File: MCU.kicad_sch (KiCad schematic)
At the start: 18 parts, among them J12 USB, U5 THVD1420DRLR, U6 CH32X035G8U6

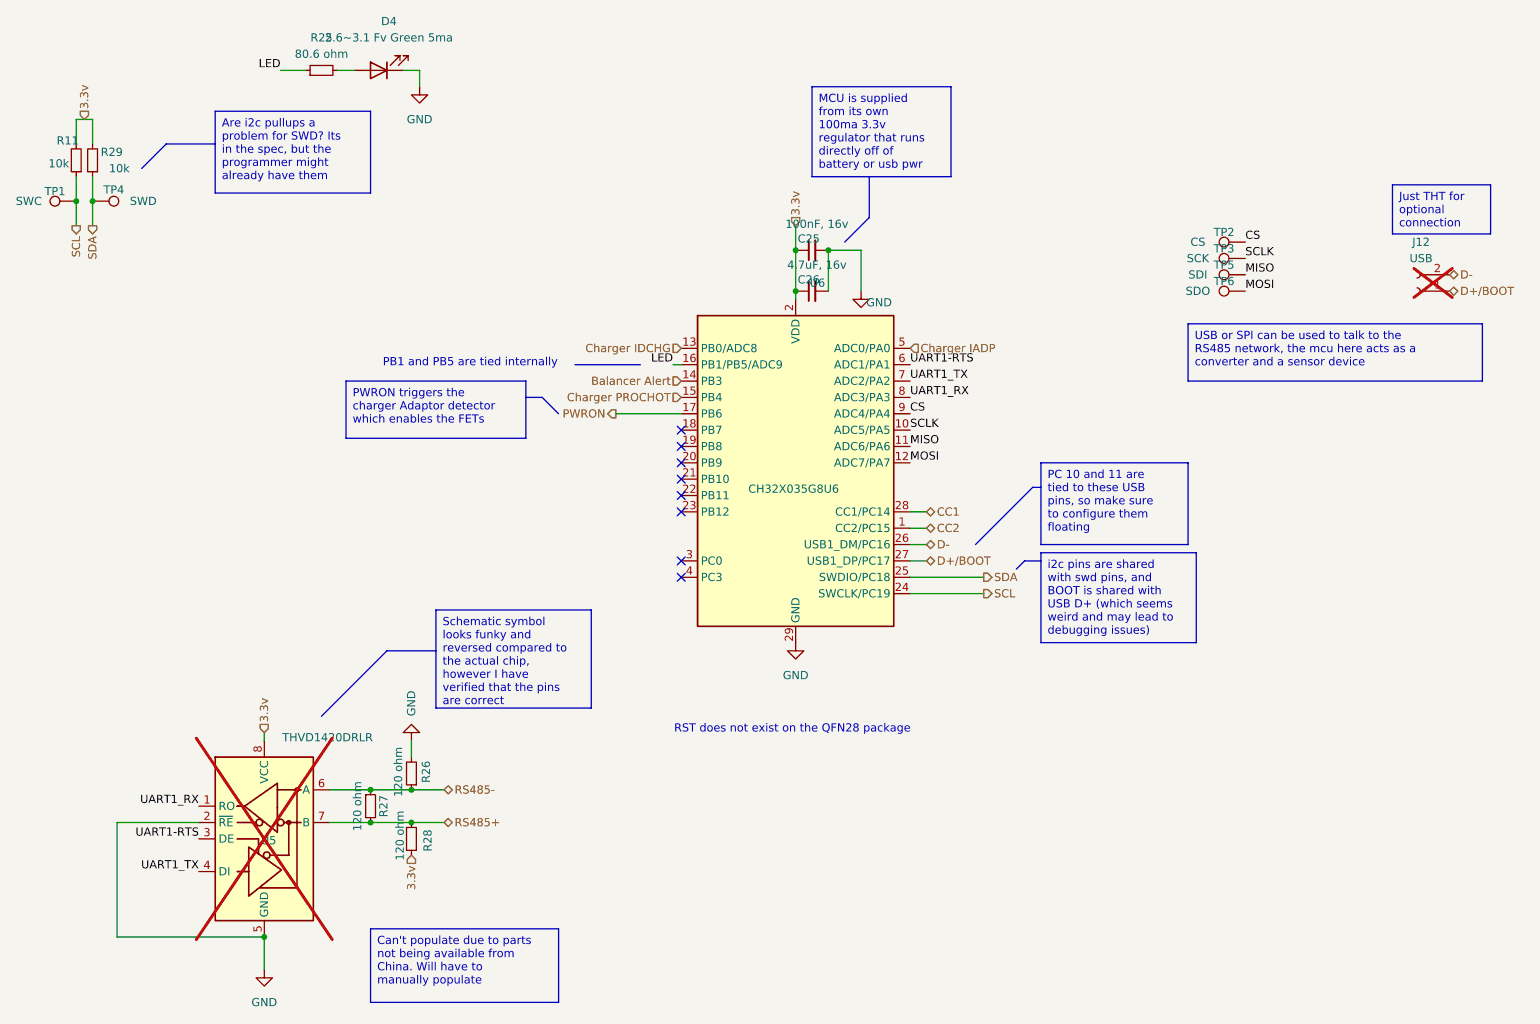
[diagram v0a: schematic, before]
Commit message: Updated to kicad 9
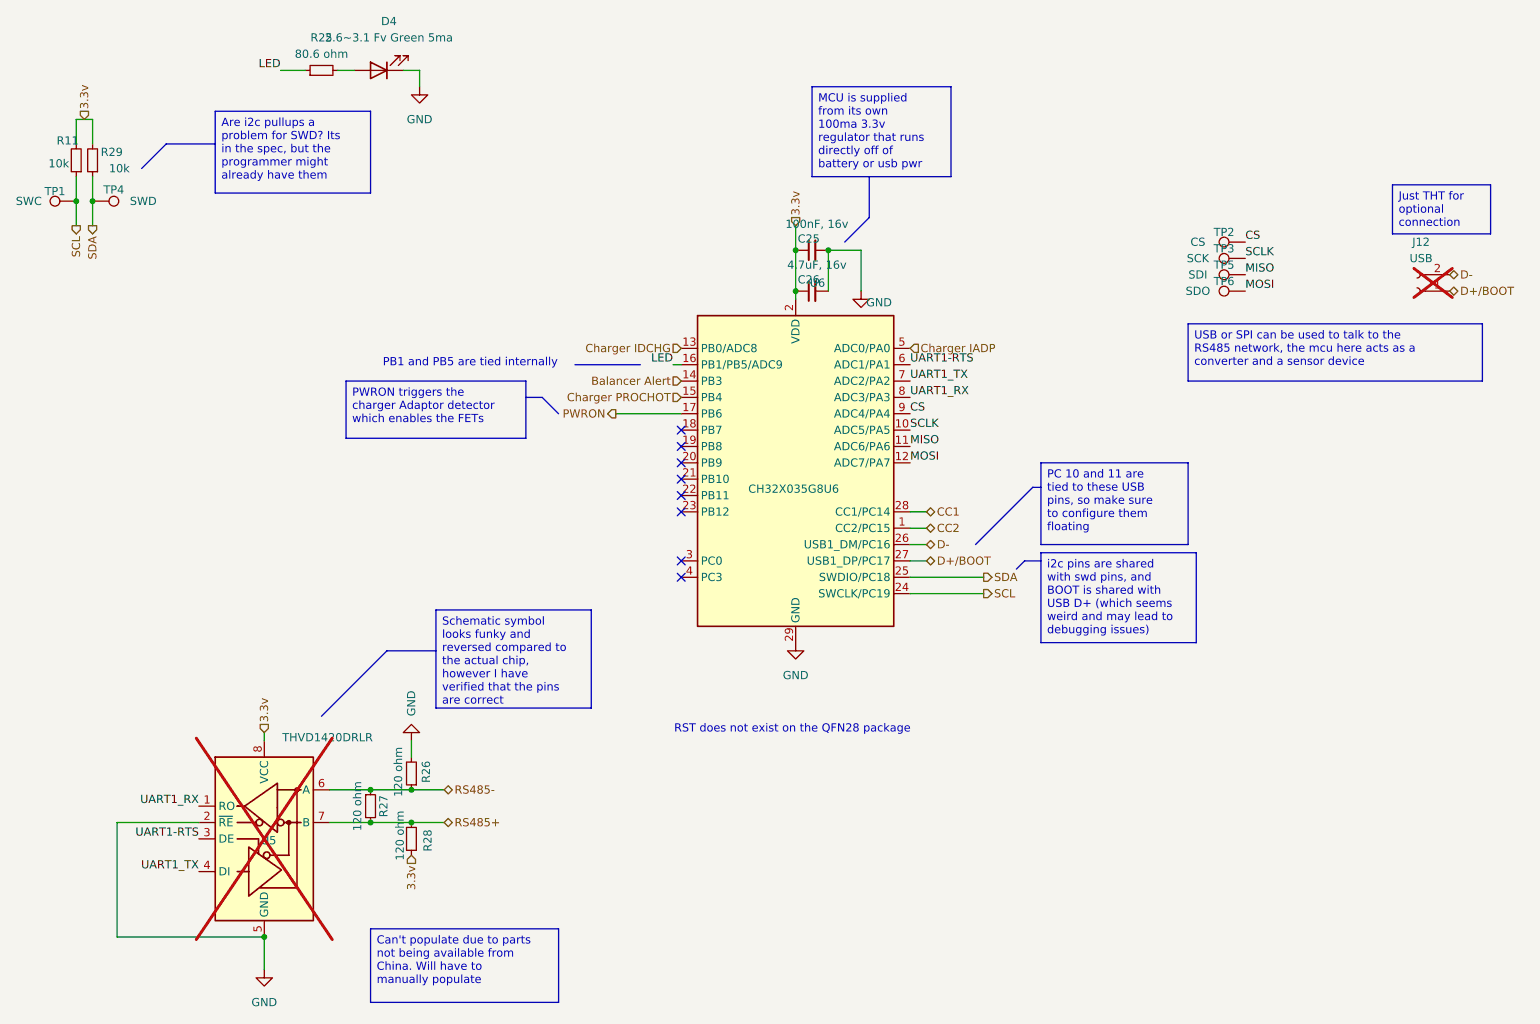
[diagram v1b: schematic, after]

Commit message: Added MCU boot button, 3v3 power enable, and pulldown on adaptor enable
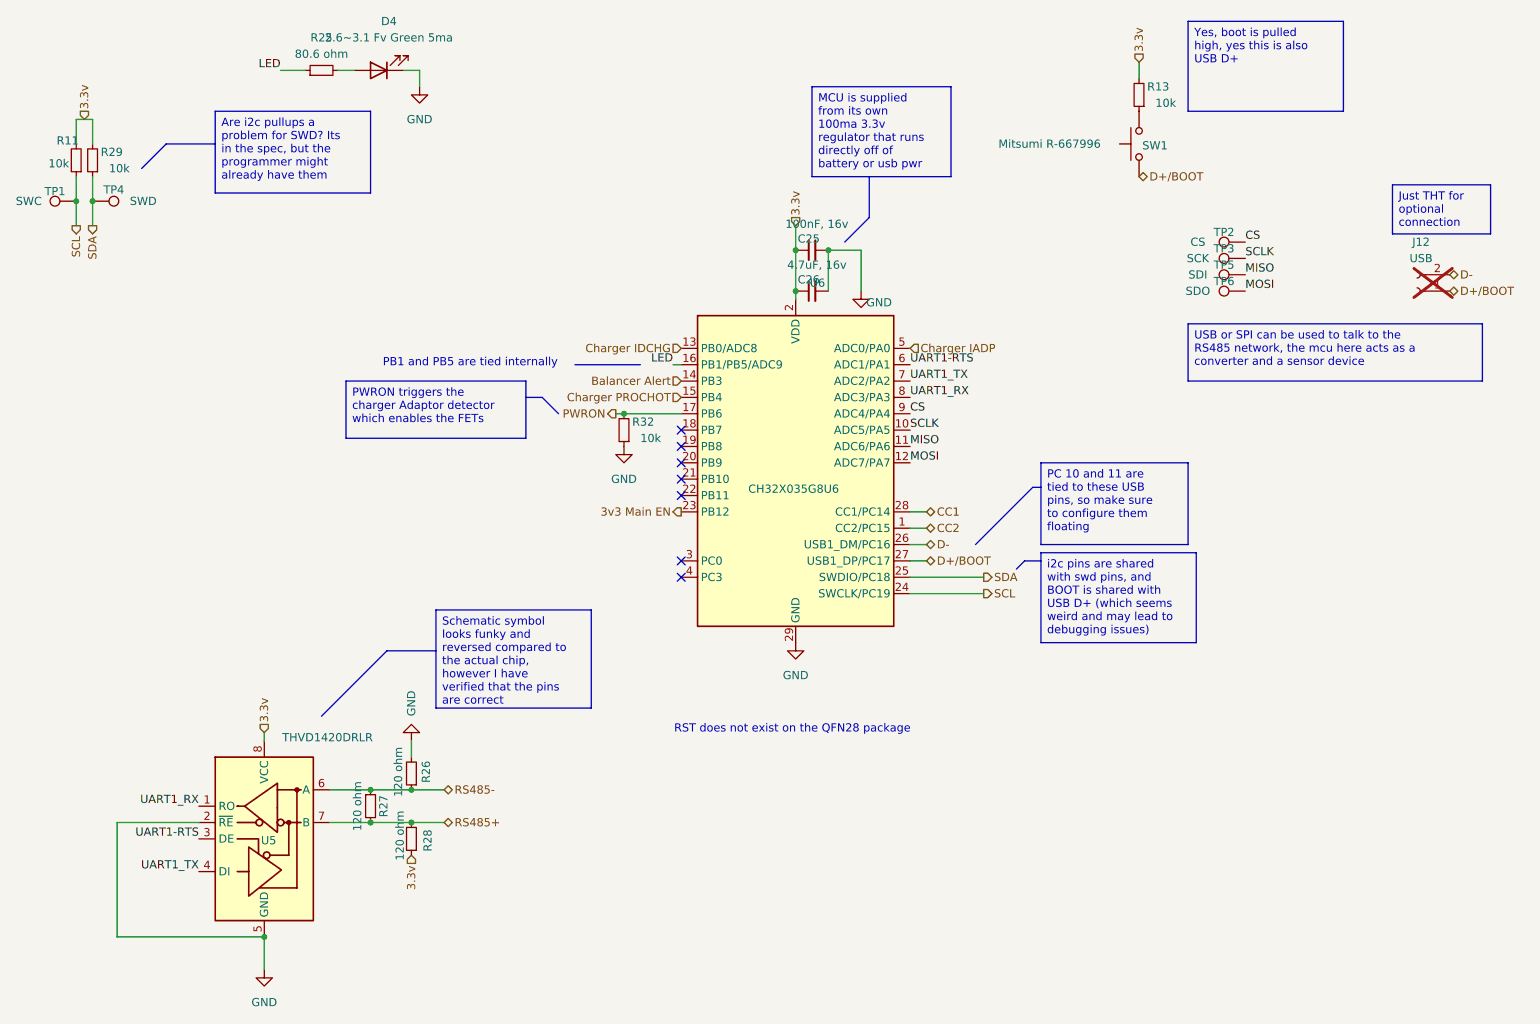
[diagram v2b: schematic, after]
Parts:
- added R13, R32: 10k, Resistor_SMD:R_0402_1005Metric, symbol Device:R_Small
- added SW1: Mitsumi R-667996, Misumi switches:R-667995_MIT, symbol Switch:SW_Push
- U5: now fitted
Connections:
- net 3.3v: now also R13.2
- net D+/BOOT: now also SW1.1
- net GND: now also R32.1
- net PWRON: now also R32.2
- net 3v3 Main EN: now reaches U6.23 (PB12)
- new net: R13.1, SW1.2
- no-connect marks 8 -> 7

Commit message: Added pdf schematics
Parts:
- U6: footprint Package_DFN_QFN:QFN-28-1EP_4x4mm_P0.4mm_EP2.8x2.8mm -> qfn_custom:QFN-28-1EP_4x4mm_P0.4mm_EP2.8x2.8mm
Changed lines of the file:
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@@
 			)
 		)
-		(property "Footprint" "Package_DFN_QFN:QFN-28-1EP_4x4mm_P0.4mm_EP2.8x2.8mm"
+		(property "Footprint" "qfn_custom:QFN-28-1EP_4x4mm_P0.4mm_EP2.8x2.8mm"
 			(at 146.05 142.24 0)
 			(effects

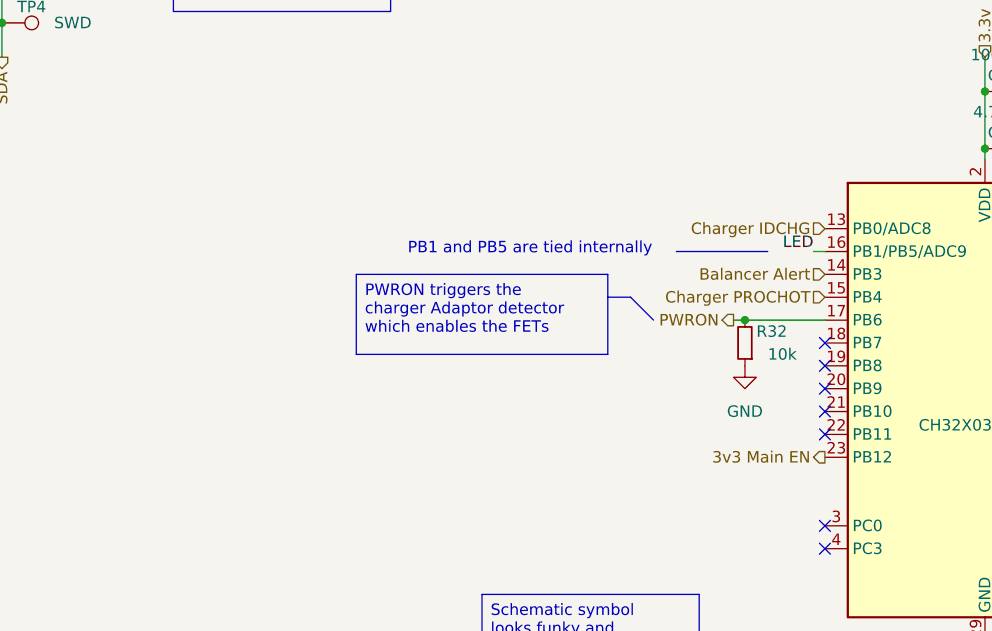
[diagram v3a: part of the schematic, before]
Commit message: Re order LED and enable pins
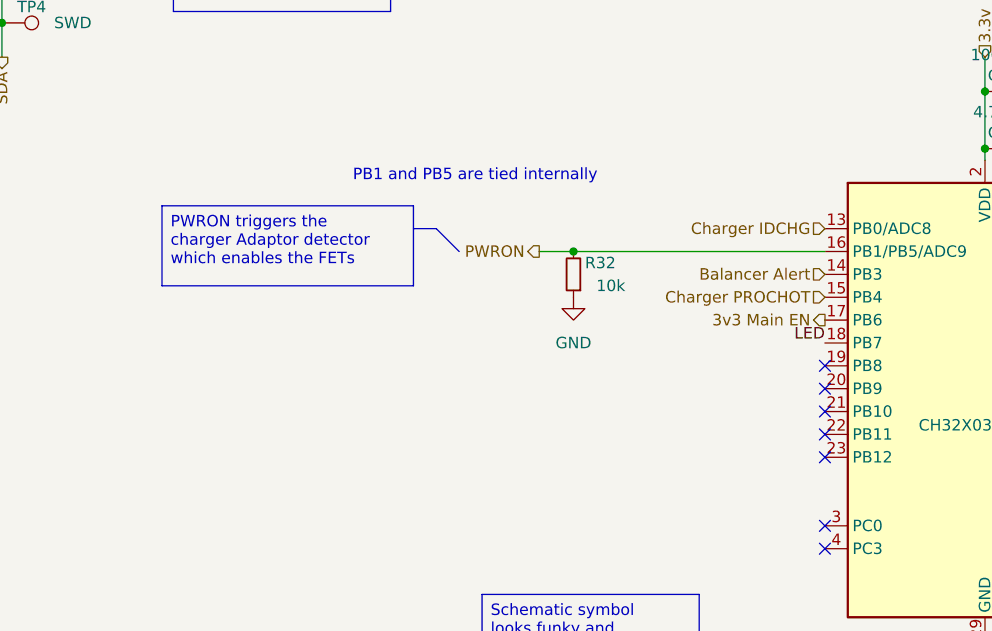
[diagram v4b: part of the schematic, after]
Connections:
- net 3v3 Main EN: now also U6.17 (PB6); no longer U6.23 (PB12)
- net LED: now also U6.18 (PB7); no longer U6.16 (PB1/PB5/ADC9)
- net PWRON: now also U6.16 (PB1/PB5/ADC9); no longer U6.17 (PB6)
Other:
- moved on the sheet: R32
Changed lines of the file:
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@@
 	(text "PB1 and PB5 are tied internally"
 		(exclude_from_sim no)
-		(at 90.424 75.946 0)
+		(at 84.328 67.818 0)
 		(effects
 			(font
@@
 	(text_box "PWRON triggers the charger Adaptor detector which enables the FETs"
 		(exclude_from_sim no)
-		(at 71.12 78.74 0)
+		(at 49.53 71.12 0)
 		(size 27.94 8.89)
 		(margins 0.9525 0.9525 0.9525 0.9525)
@@
 	)
 	(junction
-		(at 114.3 83.82)
-		(diameter 0)
-		(color 0 0 0 0)
-	)
-	(junction
 		(at 140.97 64.77)
 		(diameter 0)
@@
 		(color 0 0 0 0)
 	)
+	(junction
+		(at 95.25 76.2)
+		(diameter 0)
+		(color 0 0 0 0)
+	)
 	(no_connect
 		(at 123.19 109.22)
@@
 	)
 	(no_connect
-		(at 123.19 106.68)
+		(at 123.19 99.06)
 	)
 	(no_connect
-		(at 123.19 86.36)
+		(at 123.19 106.68)
 	)
 	(no_connect
@@
 	(polyline
 		(pts
-			(xy 101.6 81.28) (xy 104.14 83.82)
-		)
-		(stroke
-			(width 0)
-			(type default)
-		)
-	)
-	(polyline
-		(pts
-			(xy 106.68 76.2) (xy 116.84 76.2)
+			(xy 80.01 73.66) (xy 82.55 76.2)
 		)
 		(stroke
@@
 	(polyline
 		(pts
-			(xy 99.06 81.28) (xy 101.6 81.28)
+			(xy 77.47 73.66) (xy 80.01 73.66)
 		)
 		(stroke
@@
 	(wire
 		(pts
-			(xy 113.03 83.82) (xy 114.3 83.82)
+			(xy 91.44 76.2) (xy 95.25 76.2)
 		)
 		(stroke
@@
 	(wire
 		(pts
-			(xy 121.92 76.2) (xy 123.19 76.2)
-		)
-		(stroke
-			(width 0)
-			(type default)
-		)
-	)
-	(wire
-		(pts
 			(xy 74.93 147.32) (xy 68.58 147.32)
 		)
@@
 	(wire
 		(pts
-			(xy 114.3 83.82) (xy 123.19 83.82)
+			(xy 69.85 30.48) (xy 72.39 30.48)
 		)
 		(stroke
@@
 	(wire
 		(pts
-			(xy 69.85 30.48) (xy 72.39 30.48)
+			(xy 161.29 101.6) (xy 158.75 101.6)
 		)
 		(stroke
@@
 	(wire
 		(pts
-			(xy 161.29 101.6) (xy 158.75 101.6)
+			(xy 161.29 99.06) (xy 158.75 99.06)
 		)
 		(stroke
@@
 	(wire
 		(pts
-			(xy 161.29 99.06) (xy 158.75 99.06)
+			(xy 74.93 147.32) (xy 81.28 147.32)
 		)
 		(stroke
@@
 	(wire
 		(pts
-			(xy 74.93 147.32) (xy 81.28 147.32)
+			(xy 140.97 64.77) (xy 140.97 66.04)
 		)
 		(stroke
@@
 	(wire
 		(pts
-			(xy 140.97 64.77) (xy 140.97 66.04)
+			(xy 95.25 76.2) (xy 123.19 76.2)
 		)
 		(stroke
@@
 	)
 	(label "LED"
-		(at 121.92 76.2 180)
+		(at 123.19 86.36 180)
 		(effects
 			(font
@@
 	(hierarchical_label "PWRON"
 		(shape output)
-		(at 113.03 83.82 180)
+		(at 91.44 76.2 180)
 		(effects
 			(font
@@
 	(hierarchical_label "3v3 Main EN"
 		(shape output)
-		(at 123.19 99.06 180)
+		(at 123.19 83.82 180)
 		(effects
 			(font
@@
 	(symbol
 		(lib_id "power:GND")
-		(at 114.3 88.9 0)
+		(at 95.25 81.28 0)
 		(unit 1)
 		(exclude_from_sim no)
@@
 		(fields_autoplaced yes)
 		(property "Reference" "#PWR049"
-			(at 114.3 95.25 0)
+			(at 95.25 87.63 0)
 			(effects
 				(font
@@
 		)
 		(property "Value" "GND"
-			(at 114.3 93.98 0)
+			(at 95.25 86.36 0)
 			(effects
 				(font
@@
 		)
 		(property "Footprint" ""
-			(at 114.3 88.9 0)
+			(at 95.25 81.28 0)
 			(effects
 				(font
@@
 		)
 		(property "Datasheet" ""
-			(at 114.3 88.9 0)
+			(at 95.25 81.28 0)
 			(effects
 				(font
@@
 		)
 		(property "Description" "Power symbol creates a global label with name \"GND\" , ground"
-			(at 114.3 88.9 0)
+			(at 95.25 81.28 0)
 			(effects
 				(font
@@
 	(symbol
 		(lib_id "Device:R_Small")
-		(at 114.3 86.36 180)
+		(at 95.25 78.74 180)
 		(unit 1)
 		(exclude_from_sim no)
@@
 		(dnp no)
 		(property "Reference" "R32"
-			(at 115.57 85.09 0)
+			(at 96.52 77.47 0)
 			(effects
 				(font
@@
 		)
 		(property "Value" "10k"
-			(at 116.84 87.6299 0)
+			(at 97.79 80.0099 0)
 			(effects
 				(font
@@
 		)
 		(property "Footprint" "Resistor_SMD:R_0402_1005Metric"
-			(at 114.3 86.36 0)
+			(at 95.25 78.74 0)
 			(effects
 				(font
@@
 		)
 		(property "Datasheet" "~"
-			(at 114.3 86.36 0)
+			(at 95.25 78.74 0)
 			(effects
 				(font
@@
 		)
 		(property "Description" "Resistor, small symbol"
-			(at 114.3 86.36 0)
+			(at 95.25 78.74 0)
 			(effects
 				(font
@@
 		)
 		(property "LCSC" "C25744"
-			(at 115.57 85.09 0)
+			(at 96.52 77.47 0)
 			(effects
 				(font
